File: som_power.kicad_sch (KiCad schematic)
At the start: 99 parts, among them J1 Hermaphroditic_Molex_203456-0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, Q10 DMG1012T-7, Q11 DMG1012T-7, Q17 DMG1012T-7, Q18 DMG1012T-7, Q20 DMG1012T-7, Q22 DMG1012T-7, Q30 DMG1012T-7, Q37 DMG1012T-7, Q38 DMG1012T-7, Q40 DMG1012T-7, Q7 DMG1012T-7, Q8 DMG1012T-7, SW2 SW_SPDT_PCM12SMTR, U70 MAX16150A_SOT, U72 TPS3840PL30DBVR, U74 SN74LVC2G07DCKR

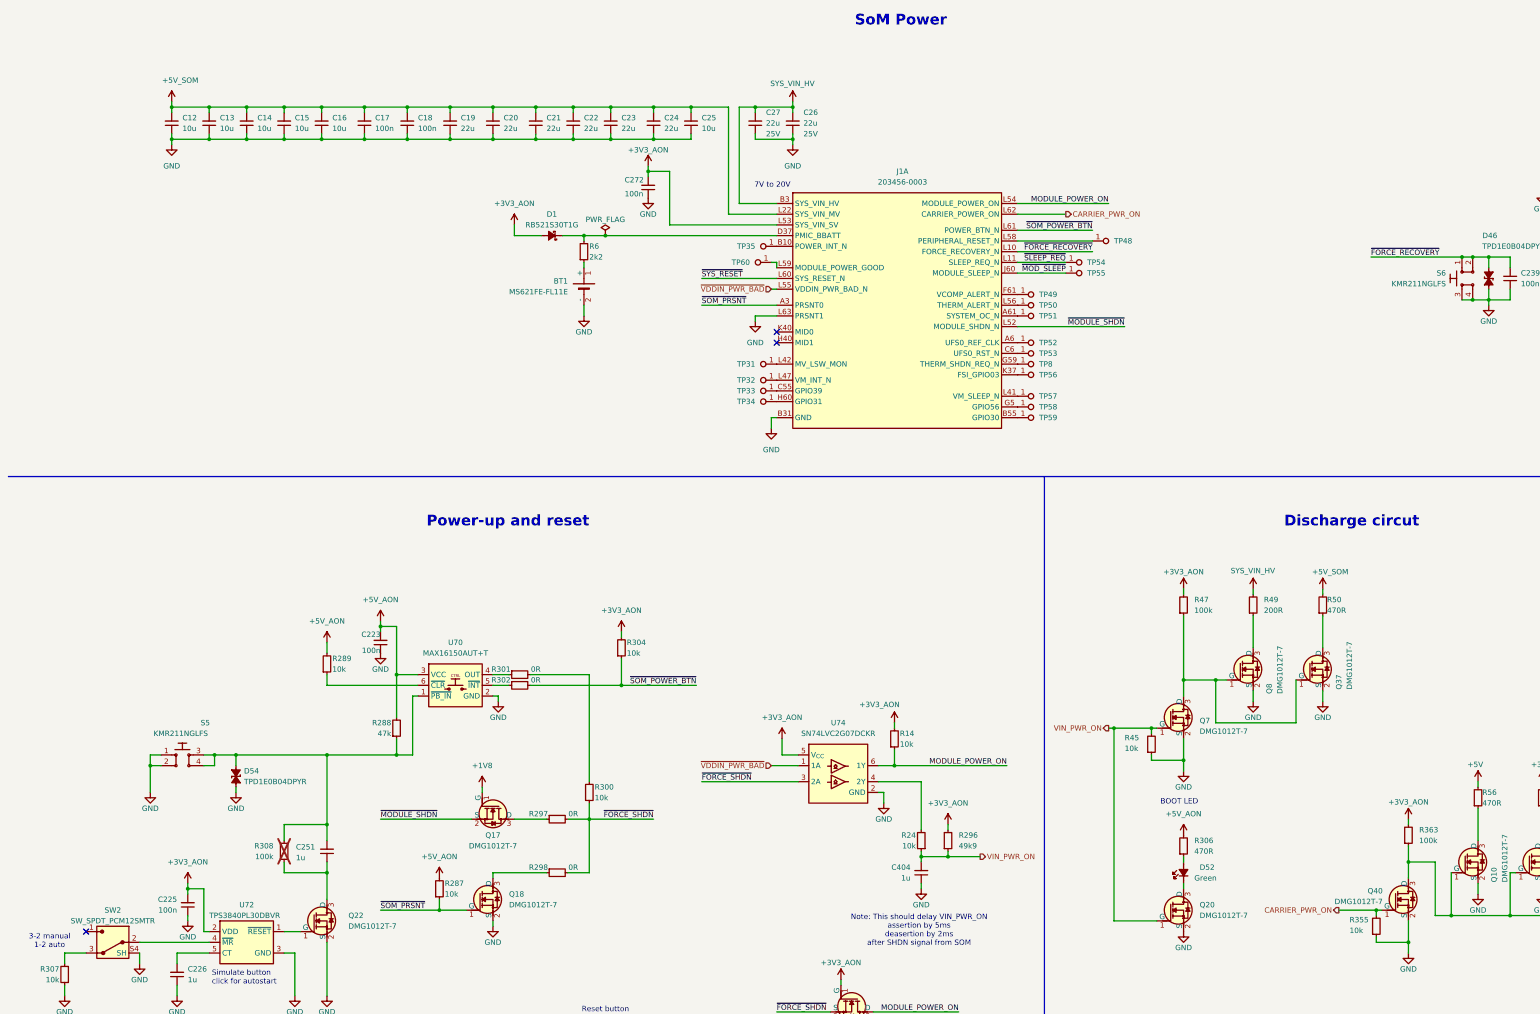
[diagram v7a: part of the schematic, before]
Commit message: [#85326] Add SoM capacitors, add testpoints
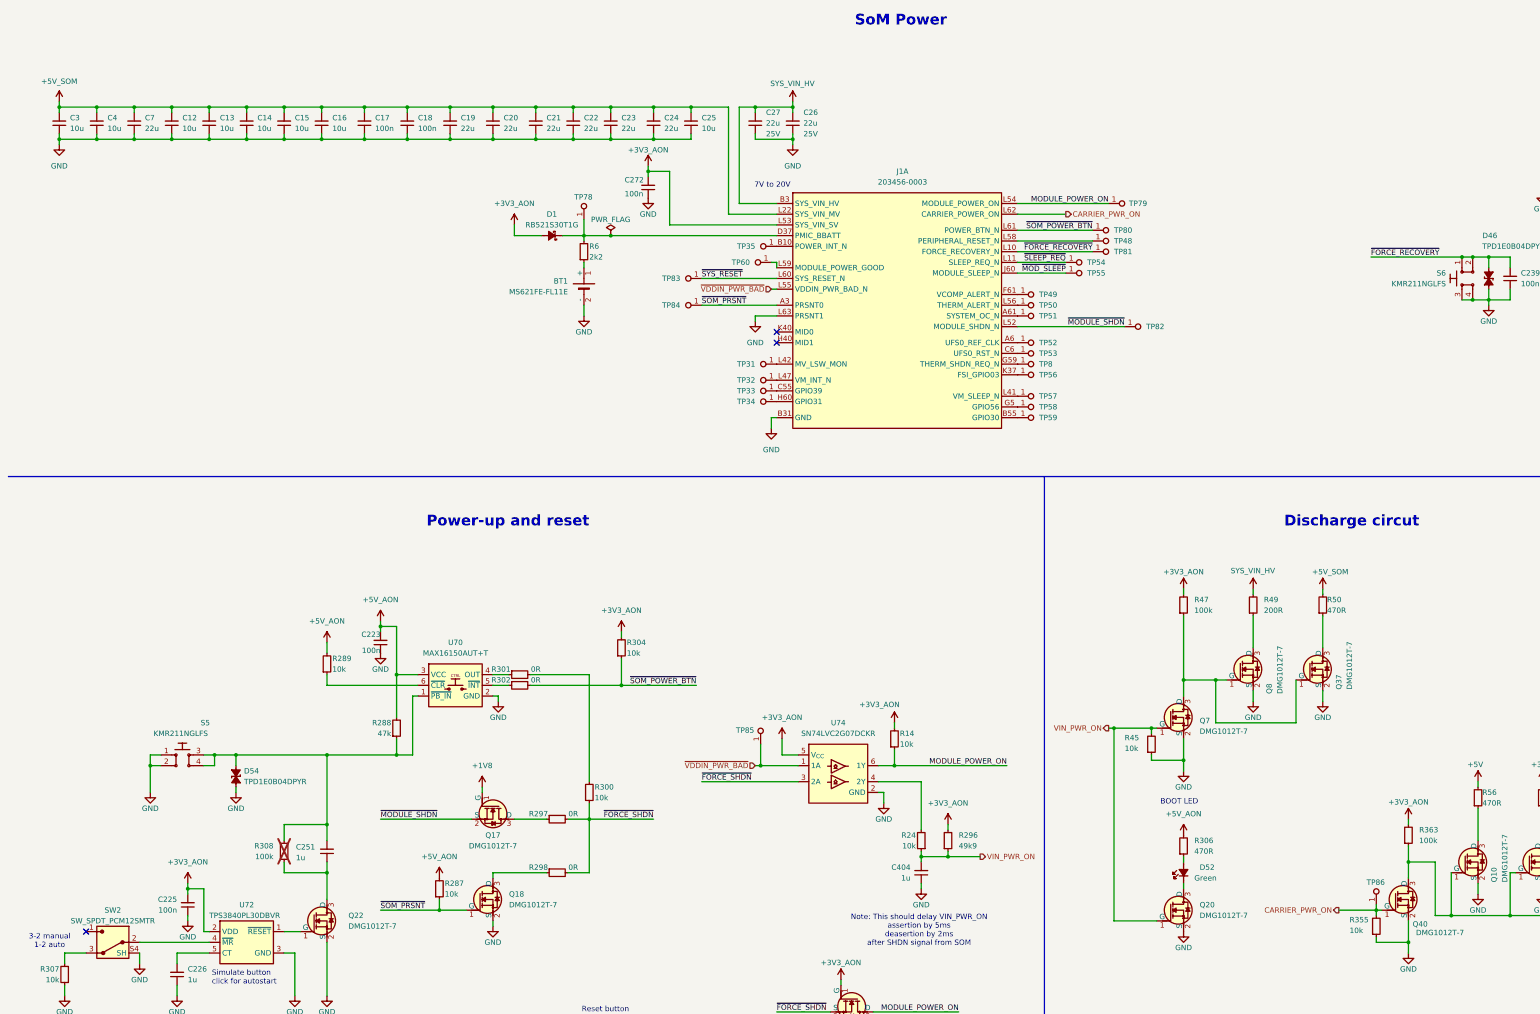
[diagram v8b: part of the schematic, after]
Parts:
- added C3, C4: C_10u_0402, antmicro-footprints:C_0402_1005Metric, symbol antmicroCapacitors0402:C_10u_0402
- added C7: C_22u_16V_0603, antmicro-footprints:C_0603_1608Metric_EIA, symbol antmicroCapacitors0603:C_22u_16V_0603
- added TP78, TP79, TP80, TP81, TP82, TP83, TP84, TP85, TP86: TP_0.75mm_SMD, antmicro-footprints:TP_SMD_0.75mm, symbol antmicroTestPoints:TP_0.75mm_SMD
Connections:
- net +5V_SOM: now also C3.2, C4.2, C7.2
- net CARRIER_PWR_ON: now also TP86.1
- net GND: now also C3.1, C4.1, C7.1
- net MODULE_POWER_ON: now also TP79.1
- net ~{FORCE_RECOVERY}: now also TP81.1
- net ~{MODULE_SHDN}: now also TP82.1
- net ~{SOM_POWER_BTN}: now also TP80.1
- net ~{SOM_PRSNT}: now also TP84.1
- net ~{SYS_RESET}: now also TP83.1
- net ~{VDDIN_PWR_BAD}: now also TP85.1
- net at D1.1 (C), J1.D37 (PMIC_BBATT), R6.2: now also TP78.1
